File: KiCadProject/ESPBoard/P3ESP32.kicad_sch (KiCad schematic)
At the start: 8 parts, among them U301 ESP32-S3-WROOM-1

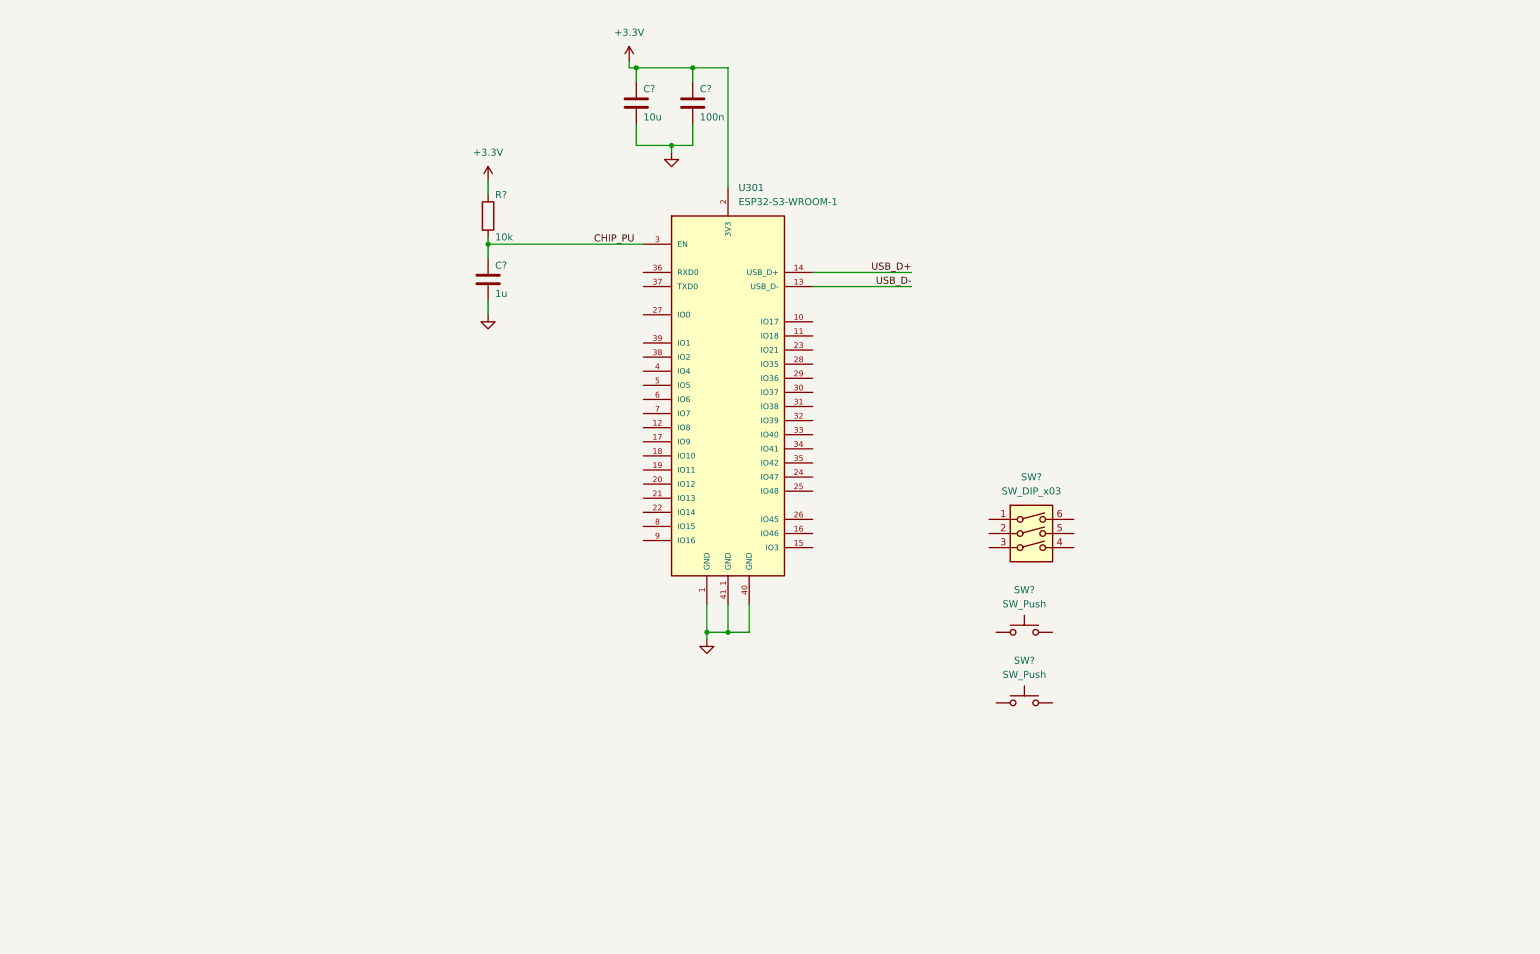
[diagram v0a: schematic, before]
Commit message: ESP board layout mostly done. Small updates to battery management board
Signed-off-by: Eldalote.Electronics <Eldalote.Electronics@gmail.com>
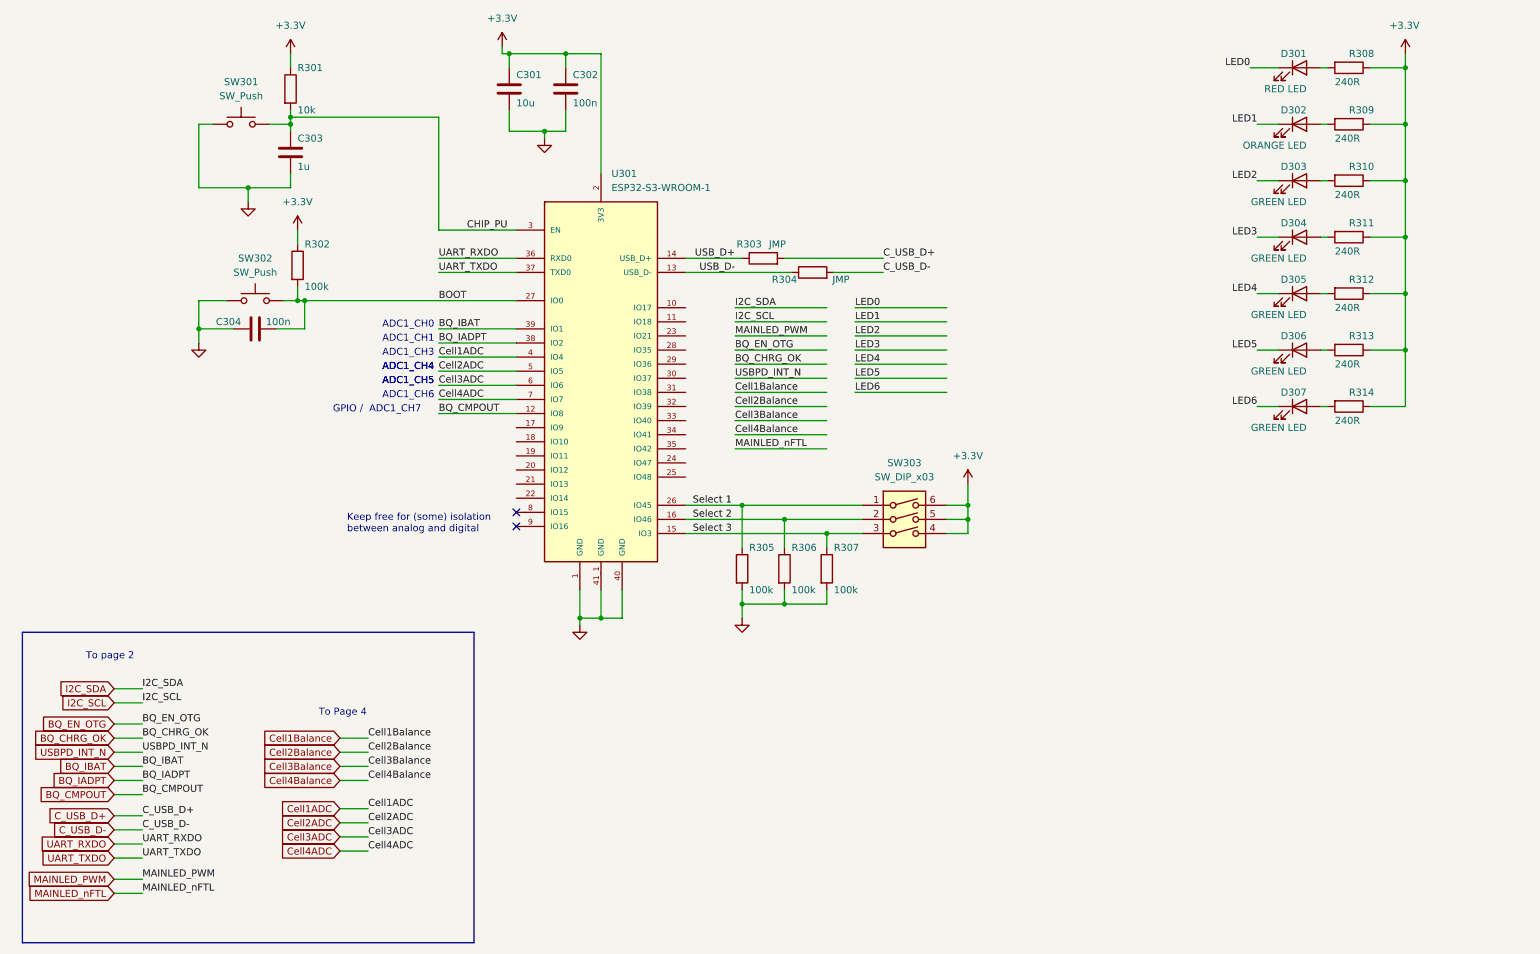
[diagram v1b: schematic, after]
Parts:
- added C304: 100n, Capacitor_SMD:C_0402_1005Metric, symbol Device:C
- added D301: RED LED, LED_SMD:LED_0603_1608Metric, symbol Device:LED
- added D302: ORANGE LED, LED_SMD:LED_0603_1608Metric, symbol Device:LED
- added D303, D304, D305, D306, D307: GREEN LED, LED_SMD:LED_0603_1608Metric, symbol Device:LED
- added R302, R305, R306, R307: 100k, Resistor_SMD:R_0402_1005Metric, symbol Device:R
- added R303, R304: JMP, Resistor_SMD:R_0402_1005Metric, symbol Device:R
- added R308, R309, R310, R311, R312, R313, R314: 240R, Resistor_SMD:R_0402_1005Metric, symbol Device:R
- C301: renamed from C?; footprint (none) -> Capacitor_SMD:C_0805_2012Metric
- C302: renamed from C?; footprint (none) -> Capacitor_SMD:C_0402_1005Metric
- C303: renamed from C?; footprint (none) -> Capacitor_SMD:C_0603_1608Metric
- R301: renamed from R?; footprint (none) -> Resistor_SMD:R_0402_1005Metric
- gave numbers to parts that had none: 3
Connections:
- net +3.3V: now also SW303.4, SW303.5, SW303.6, R302.1, R308.1, R309.1, R310.1, R311.1, R312.1, R313.1, R314.1
- net CHIP_PU: now also SW301.2
- net GND: now also SW301.1, SW302.1, C304.1, R305.2, R306.2, R307.2
- net USB_D+: now also R303.1
- net USB_D-: now also R304.1
- net Select 1: now reaches SW303.1
- net Select 1: now also U301.26 (IO45), R305.1
- net Select 2: now reaches SW303.2
- net Select 2: now also U301.16 (IO46), R306.1
- net Select 3: now reaches SW303.3
- net Select 3: now also U301.15 (IO3), R307.1
- net BOOT: now reaches SW302.2
- net BOOT: now also U301.27 (IO0), C304.2, R302.2
- net BQ_CMPOUT: now reaches U301.12 (IO8)
- net UART_RXDO: now reaches U301.36 (RXD0)
- net UART_TXDO: now reaches U301.37 (TXD0)
- net BQ_IADPT: now reaches U301.38 (IO2)
- net BQ_IBAT: now reaches U301.39 (IO1)
- net Cell1ADC: now reaches U301.4 (IO4)
- net Cell2ADC: now reaches U301.5 (IO5)
- net Cell3ADC: now reaches U301.6 (IO6)
- net Cell4ADC: now reaches U301.7 (IO7)
- new net: D302.2 (A), R309.2
- new net: D301.2 (A), R308.2
- new net: D306.2 (A), R313.2
- new net: D303.2 (A), R310.2
- new net: D304.2 (A), R311.2
- new net: D305.2 (A), R312.2
- new net: D307.2 (A), R314.2
- new net C_USB_D+: R303.2
- new net C_USB_D-: R304.2
- new net LED0: D301.1 (K)
- new net LED1: D302.1 (K)
- new net LED2: D303.1 (K)
- new net LED3: D304.1 (K)
- new net LED4: D305.1 (K)
- new net LED5: D306.1 (K)
- new net LED6: D307.1 (K)
- no-connect marks 0 -> 2
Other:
- note added: "ADC1_CH0"
- note added: "ADC1_CH1"
- note added: "ADC1_CH3"
- note added: "ADC1_CH4"
- note added: "ADC1_CH5"
- note added: "ADC1_CH6"
- note added: "GPIO / ADC1_CH7"
- note added: "Keep free for (some) isolation between analog and digital"
- note added: "To Page 4"
- note added: "To page 2"
- moved on the sheet: C301, C302, C303, R301, SW301, SW302, SW303, U301

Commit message: Tweaking
Signed-off-by: Eldalote.Electronics <Eldalote.Electronics@gmail.com>
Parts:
- removed SW303: SW_DIP_x03, symbol Switch:SW_DIP_x03
- added R315, R316, R317: DNP, Resistor_SMD:R_0402_1005Metric, symbol Device:R
- SW301, SW302: footprint (none) -> Button_Switch_SMD:SW_Push_1P1T_NO_6x6mm_H9.5mm
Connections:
- net +3.3V: now also R315.1, R316.1, R317.1
- net Select 1: now also R315.2
- net Select 2: now also R316.2
- net Select 3: now also R317.2
- net L1a: now reaches D302.2 (A), R309.2
- net L0a: now reaches D301.2 (A), R308.2
- net L5a: now reaches D306.2 (A), R313.2
- net L2a: now reaches D303.2 (A), R310.2
- net L3a: now reaches D304.2 (A), R311.2
- net L4a: now reaches D305.2 (A), R312.2
- net L6a: now reaches D307.2 (A), R314.2
- net BOOT renamed BOOT/USER1

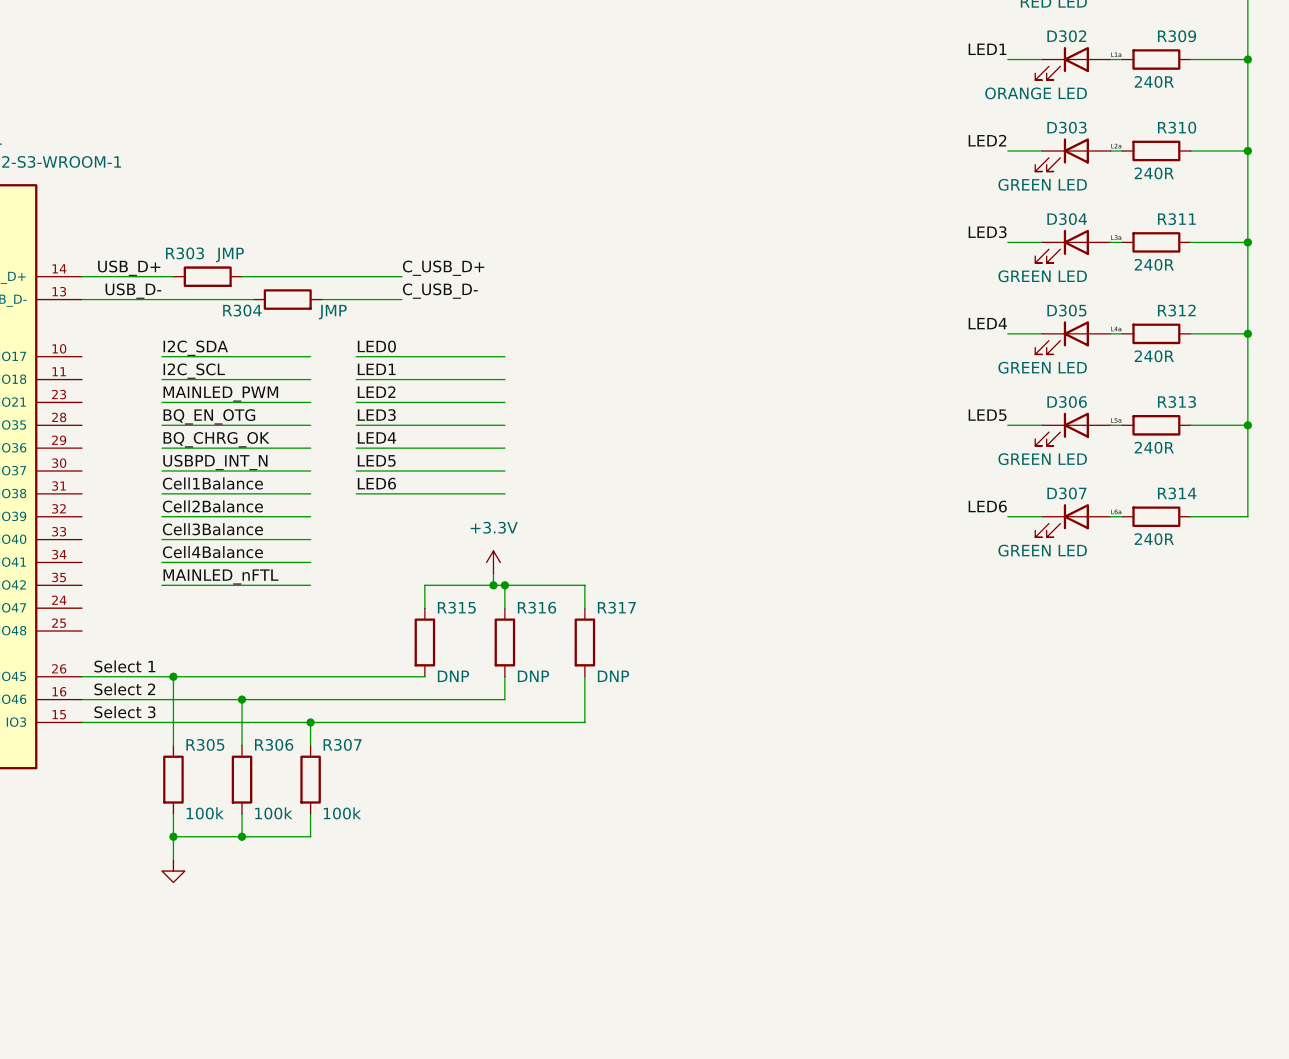
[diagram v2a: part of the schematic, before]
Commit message: Final touches before component order and PCB layout
Signed-off-by: Eldalote.Electronics <Eldalote.Electronics@gmail.com>
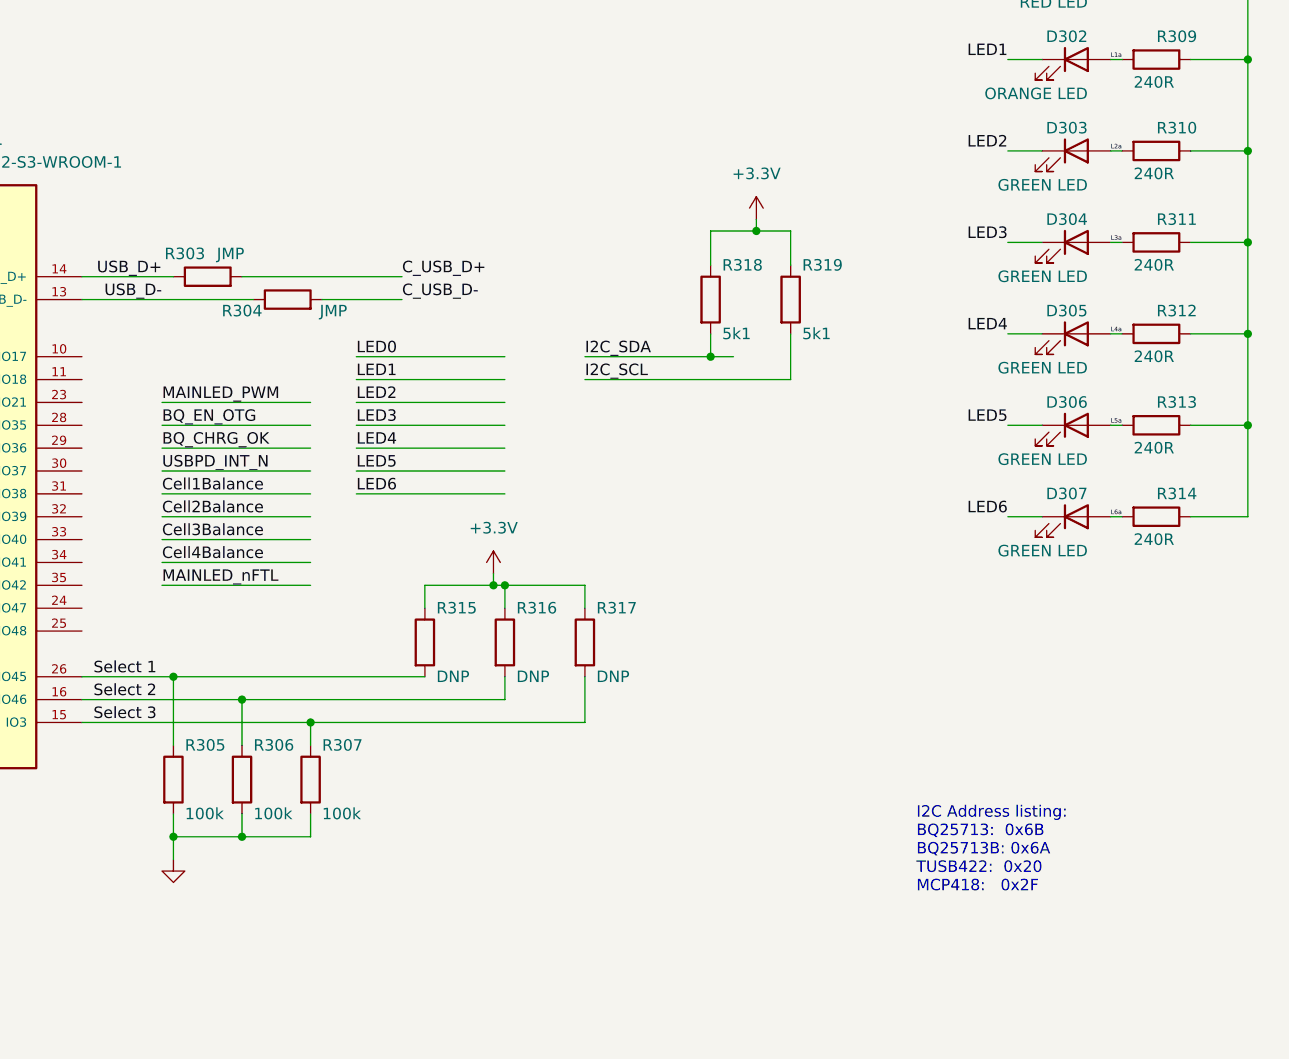
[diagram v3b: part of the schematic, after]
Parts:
- added R318, R319: 5k1, Resistor_SMD:R_0402_1005Metric, symbol Device:R
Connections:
- net +3.3V: now also R318.1, R319.1
- net I2C_SCL: now also R319.2
- net I2C_SDA: now also R318.2
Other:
- note added: "I2C Address listing: BQ25713: 0x6B BQ25713B: 0x6A TUSB422: 0x20 MCP418: 0x2F"
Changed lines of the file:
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@@
   (junction (at 144.78 134.62) (diameter 0) (color 0 0 0 0)
   )
+  (junction (at 209.55 67.31) (diameter 0) (color 0 0 0 0)
+  )
   (junction (at 119.38 137.16) (diameter 0) (color 0 0 0 0)
   )
@@
   )
   (junction (at 115.57 137.16) (diameter 0) (color 0 0 0 0)
+  )
+  (junction (at 204.47 81.28) (diameter 0) (color 0 0 0 0)
   )
   (junction (at 66.04 80.01) (diameter 0) (color 0 0 0 0)
@@
   (no_connect (at 104.14 118.11))
   (no_connect (at 104.14 120.65))
+  (wire (pts (xy 204.47 67.31) (xy 209.55 67.31))
+    (stroke (width 0) (type default) (color 0 0 0 0))
+  )
   (wire (pts (xy 90.17 67.31) (xy 104.14 67.31))
     (stroke (width 0) (type default) (color 0 0 0 0))
@@
     (stroke (width 0) (type default) (color 0 0 0 0))
   )
+  (wire (pts (xy 204.47 78.74) (xy 204.47 81.28))
+    (stroke (width 0) (type default) (color 0 0 0 0))
+  )
   (wire (pts (xy 264.16 48.26) (xy 257.81 48.26))
     (stroke (width 0) (type default) (color 0 0 0 0))
@@
     (stroke (width 0) (type default) (color 0 0 0 0))
   )
-  (wire (pts (xy 143.51 83.82) (xy 160.02 83.82))
+  (wire (pts (xy 190.5 83.82) (xy 213.36 83.82))
     (stroke (width 0) (type default) (color 0 0 0 0))
   )
@@
     (stroke (width 0) (type default) (color 0 0 0 0))
   )
+  (wire (pts (xy 204.47 71.12) (xy 204.47 67.31))
+    (stroke (width 0) (type default) (color 0 0 0 0))
+  )
   (wire (pts (xy 63.5 46.99) (xy 63.5 48.26))
     (stroke (width 0) (type default) (color 0 0 0 0))
@@
     (stroke (width 0) (type default) (color 0 0 0 0))
   )
+  (wire (pts (xy 204.47 81.28) (xy 207.01 81.28))
+    (stroke (width 0) (type default) (color 0 0 0 0))
+  )
   (wire (pts (xy 250.19 58.42) (xy 248.92 58.42))
     (stroke (width 0) (type default) (color 0 0 0 0))
@@
     (stroke (width 0) (type default) (color 0 0 0 0))
   )
+  (wire (pts (xy 213.36 71.12) (xy 213.36 67.31))
+    (stroke (width 0) (type default) (color 0 0 0 0))
+  )
   (wire (pts (xy 66.04 85.09) (xy 66.04 80.01))
     (stroke (width 0) (type default) (color 0 0 0 0))
@@
     (stroke (width 0) (type default) (color 0 0 0 0))
   )
+  (wire (pts (xy 209.55 66.04) (xy 209.55 67.31))
+    (stroke (width 0) (type default) (color 0 0 0 0))
+  )
   (wire (pts (xy 46.99 59.69) (xy 55.88 59.69))
     (stroke (width 0) (type default) (color 0 0 0 0))
@@
     (stroke (width 0) (type default) (color 0 0 0 0))
   )
+  (wire (pts (xy 213.36 67.31) (xy 209.55 67.31))
+    (stroke (width 0) (type default) (color 0 0 0 0))
+  )
   (polyline (pts (xy 15.24 195.58) (xy 96.52 195.58))
     (stroke (width 0) (type default) (color 0 0 0 0))
@@
     (stroke (width 0) (type default) (color 0 0 0 0))
   )
-  (wire (pts (xy 143.51 81.28) (xy 160.02 81.28))
+  (wire (pts (xy 190.5 81.28) (xy 204.47 81.28))
     (stroke (width 0) (type default) (color 0 0 0 0))
   )
@@
     (stroke (width 0) (type default) (color 0 0 0 0))
   )
+  (wire (pts (xy 213.36 83.82) (xy 213.36 78.74))
+    (stroke (width 0) (type default) (color 0 0 0 0))
+  )
   (wire (pts (xy 152.4 134.62) (xy 160.02 134.62))
     (stroke (width 0) (type default) (color 0 0 0 0))
@@
   )
   (text "To page 2" (at 26.67 144.78 0)
+    (effects (font (size 1.27 1.27)) (justify left bottom))
+  )
+  (text "I2C Address listing:\nBQ25713:  0x6B\nBQ25713B: 0x6A\nTUSB422:  0x20\nMCP418:   0x2F"
+    (at 227.33 140.97 0)
     (effects (font (size 1.27 1.27)) (justify left bottom))
   )
@@
     (effects (font (size 0.5 0.5)) (justify left bottom))
   )
-  (label "I2C_SDA" (at 143.51 81.28 0)
+  (label "I2C_SDA" (at 190.5 81.28 0)
     (effects (font (size 1.27 1.27)) (justify left bottom))
   )
@@
     (effects (font (size 1.27 1.27)) (justify left bottom))
   )
-  (label "I2C_SCL" (at 143.51 83.82 0)
+  (label "I2C_SCL" (at 190.5 83.82 0)
     (effects (font (size 1.27 1.27)) (justify left bottom))
   )
@@
     (pin "1")
     (pin "2")
+  )
+  (symbol (lib_id "power:+3.3V") (at 209.55 66.04 0) (unit 1)
+    (in_bom yes) (on_board yes) (fields_autoplaced)
+    (property "Reference" "#PWR?" (id 0) (at 209.55 69.85 0)
+      (effects (font (size 1.27 1.27)) hide)
+    )
+    (property "Value" "+3.3V" (id 1) (at 209.55 60.96 0))
+    (property "Footprint" "" (id 2) (at 209.55 66.04 0)
+      (effects (font (size 1.27 1.27)) hide)
+    )
+    (property "Datasheet" "" (id 3) (at 209.55 66.04 0)
+      (effects (font (size 1.27 1.27)) hide)
+    )
+    (pin "1")
   )
   (symbol (lib_id "Device:C") (at 113.03 41.91 0) (unit 1)
@@
     (pin "1")
   )
+  (symbol (lib_id "Device:R") (at 204.47 74.93 0) (unit 1)
+    (in_bom yes) (on_board yes)
+    (property "Reference" "R318" (id 0) (at 205.74 71.12 0)
+      (effects (font (size 1.27 1.27)) (justify left))
+    )
+    (property "Value" "5k1" (id 1) (at 205.74 78.74 0)
+      (effects (font (size 1.27 1.27)) (justify left))
+    )
+    (property "Footprint" "Resistor_SMD:R_0402_1005Metric" (id 2) (at 202.692 74.93 90)
+      (effects (font (size 1.27 1.27)) hide)
+    )
+    (property "Datasheet" "~" (id 3) (at 204.47 74.93 0)
+      (effects (font (size 1.27 1.27)) hide)
+    )
+    (pin "1")
+    (pin "2")
+  )
+  (symbol (lib_id "Device:R") (at 213.36 74.93 0) (unit 1)
+    (in_bom yes) (on_board yes)
+    (property "Reference" "R319" (id 0) (at 214.63 71.12 0)
+      (effects (font (size 1.27 1.27)) (justify left))
+    )
+    (property "Value" "5k1" (id 1) (at 214.63 78.74 0)
+      (effects (font (size 1.27 1.27)) (justify left))
+    )
+    (property "Footprint" "Resistor_SMD:R_0402_1005Metric" (id 2) (at 211.582 74.93 90)
+      (effects (font (size 1.27 1.27)) hide)
+    )
+    (property "Datasheet" "~" (id 3) (at 213.36 74.93 0)
+      (effects (font (size 1.27 1.27)) hide)
+    )
+    (pin "1")
+    (pin "2")
+  )
   (symbol (lib_id "Device:R") (at 254 99.06 270) (unit 1)
